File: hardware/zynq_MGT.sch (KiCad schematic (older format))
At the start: 6 parts, among them U201 xc7z030sbg485

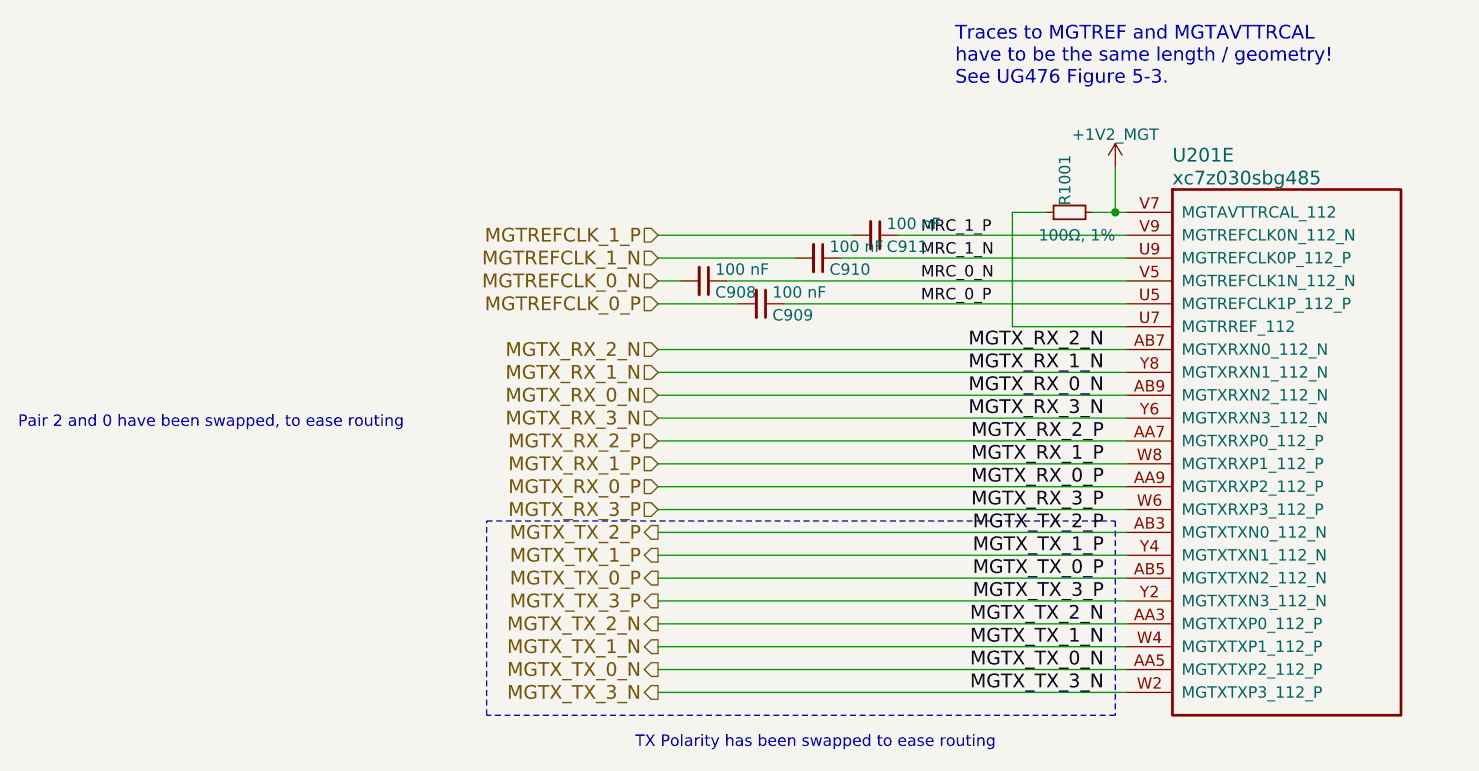
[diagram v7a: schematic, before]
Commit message: WIP: routing the HF Part of the Camera Connector. I have to move the clock away from the left border.
TODO: Fix DDR3 RAM.
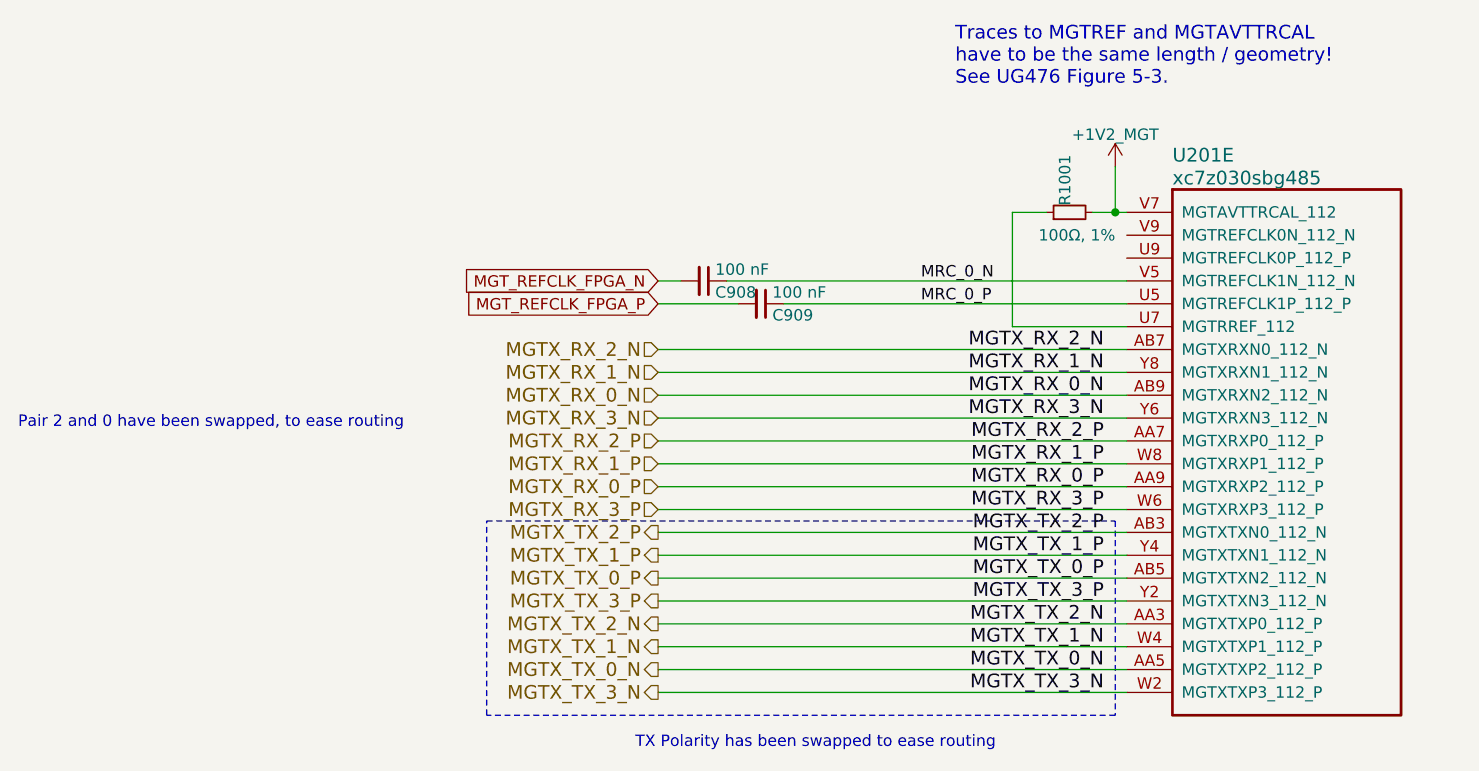
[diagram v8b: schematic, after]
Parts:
- removed C910, C911: 100 nF, Capacitor_SMD:C_0201_0603Metric, symbol Device:C_Small
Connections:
- net MGTREFCLK_0_N renamed MGT_REFCLK_FPGA_N
- net MGTREFCLK_0_P renamed MGT_REFCLK_FPGA_P
- net MRC_1_N: no longer names the net of U201.U9 (MGTREFCLK0P_112_P)
- net MRC_1_P: no longer names the net of U201.V9 (MGTREFCLK0N_112_N)
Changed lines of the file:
@@
 $Descr A4 11693 8268
 encoding utf-8
-Sheet 9 21
+Sheet 8 21
 Title ""
 Date ""
@@
 Text HLabel 3300 3850 0    60   Output ~ 0
 MGTX_TX_3_P
-Text HLabel 3300 2450 0    60   Input ~ 0
-MGTREFCLK_0_N
-Text HLabel 3300 2550 0    60   Input ~ 0
-MGTREFCLK_0_P
-Text HLabel 3300 2350 0    60   Input ~ 0
-MGTREFCLK_1_N
-Text HLabel 3300 2250 0    60   Input ~ 0
-MGTREFCLK_1_P
 Wire Wire Line
 	3600 2450 5350 2450
@@
 	3850 2550 5350 2550
 Wire Wire Line
-	4100 2350 5350 2350
-Wire Wire Line
-	4350 2250 5350 2250
-Wire Wire Line
 	3300 2450 3400 2450
 Wire Wire Line
 	3300 2550 3650 2550
-Wire Wire Line
-	3300 2350 3900 2350
-Wire Wire Line
-	3300 2250 4150 2250
 Wire Wire Line
 	3300 2950 5350 2950
@@
 	0    1    1    0
 $EndComp
-$Comp
-L Device:C_Small C910
-U 1 1 5BB23143
-P 4000 2350
-F 0 "C910" V 4050 2400 50  0000 L CNN
-F 1 "100 nF" V 3950 2400 50  0000 L CNN
-F 2 "Capacitor_SMD:C_0201_0603Metric" H 4000 2350 50  0001 C CNN
-F 3 "http://search.murata.co.jp/Ceramy/image/img/A01X/G101/ENG/GRM033R60J104KE19-01.pdf" H 4000 2350 50  0001 C CNN
-F 4 "Murata Electronics North America" H 4000 2350 60  0001 C CNN "MFG Name"
-F 5 "GRM033R60J104KE19D" H 4000 2350 60  0001 C CNN "MFG Part Num"
-F 6 "490-3167-1-ND" H 4000 2350 60  0001 C CNN "Digikey"
-F 7 "1" V 4000 2350 60  0001 C CNN "Populated"
-F 8 "SPEC" H 4000 2350 60  0001 C CNN "Source"
-	1    4000 2350
-	0    1    1    0
-$EndComp
-$Comp
-L Device:C_Small C911
-U 1 1 5BB231AA
-P 4250 2250
-F 0 "C911" V 4300 2300 50  0000 L CNN
-F 1 "100 nF" V 4200 2300 50  0000 L CNN
-F 2 "Capacitor_SMD:C_0201_0603Metric" H 4250 2250 50  0001 C CNN
-F 3 "http://search.murata.co.jp/Ceramy/image/img/A01X/G101/ENG/GRM033R60J104KE19-01.pdf" H 4250 2250 50  0001 C CNN
-F 4 "Murata Electronics North America" H 4250 2250 60  0001 C CNN "MFG Name"
-F 5 "GRM033R60J104KE19D" H 4250 2250 60  0001 C CNN "MFG Part Num"
-F 6 "490-3167-1-ND" H 4250 2250 60  0001 C CNN "Digikey"
-F 7 "1" V 4250 2250 60  0001 C CNN "Populated"
-F 8 "SPEC" H 4250 2250 60  0001 C CNN "Source"
-	1    4250 2250
-	0    1    1    0
-$EndComp
-Text Label 4450 2250 0    50   ~ 0
-MRC_1_P
-Text Label 4450 2350 0    50   ~ 0
-MRC_1_N
 Text Label 4450 2550 0    50   ~ 0
 MRC_0_P
 Text Label 4450 2450 0    50   ~ 0
 MRC_0_N
+Text GLabel 3300 2450 0    50   Input ~ 0
+MGT_REFCLK_FPGA_N
+Text GLabel 3300 2550 0    50   Input ~ 0
+MGT_REFCLK_FPGA_P
 $EndSCHEMATC
